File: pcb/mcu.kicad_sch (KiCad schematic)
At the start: 28 parts, among them U1 W25Q128JVS, U2 RP2040, Y1 ABM8AIG-12.000MHZ-12-2Z-T3

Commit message: Start routing rev. A
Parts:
- U1: footprint Package_SO:SOIC-8_5.23x5.23mm_P1.27mm -> Package_SO:SOIC-8_5.275x5.275mm_P1.27mm
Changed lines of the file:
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@@
 			)
 		)
-		(property "Footprint" "Package_SO:SOIC-8_5.23x5.23mm_P1.27mm"
+		(property "Footprint" "Package_SO:SOIC-8_5.275x5.275mm_P1.27mm"
 			(at 38.1 72.39 0)
 			(effects

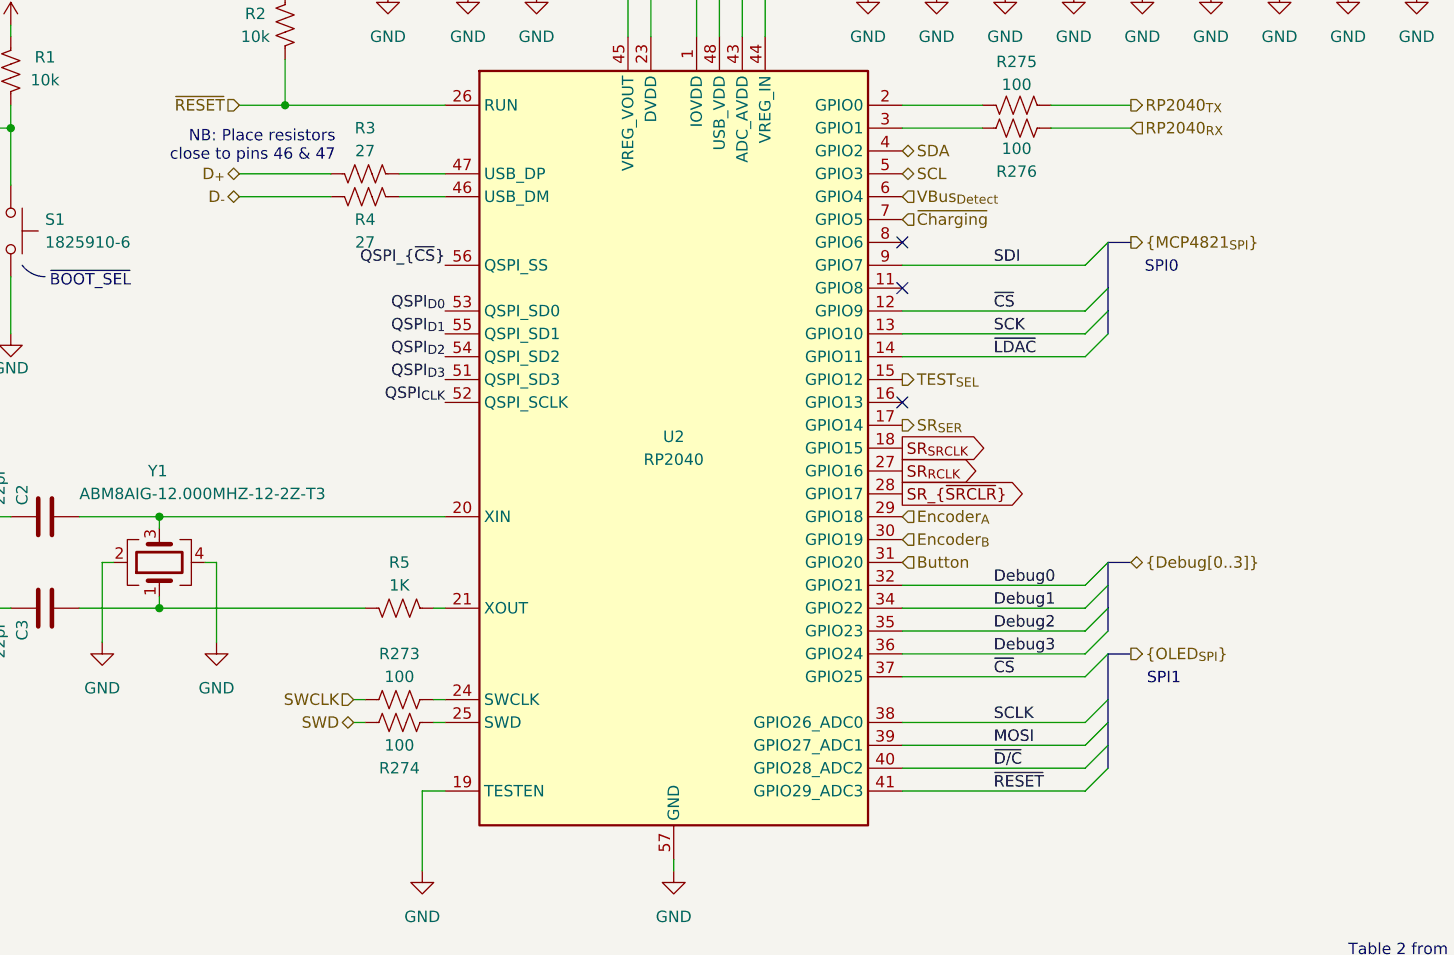
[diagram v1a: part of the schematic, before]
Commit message: Routing nearly complete
- Power switch is too tall I think
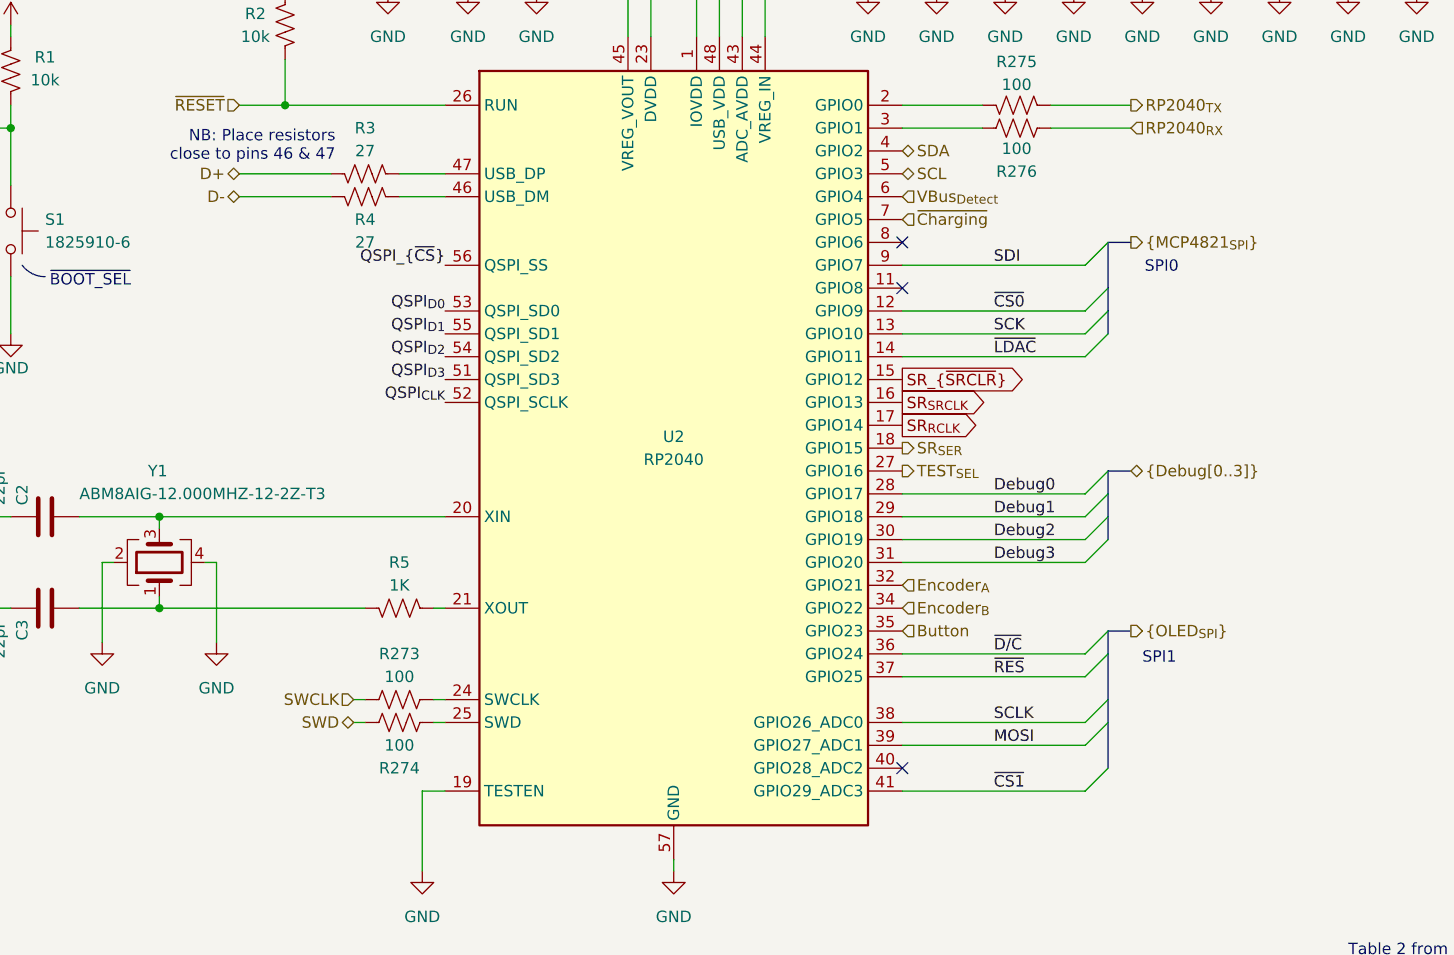
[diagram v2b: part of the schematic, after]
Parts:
- C1, C10, C11, C12, C13, C14, C5, C6, C7, C8, C9: TempCo (none) -> X7R
- C15, C4: TempCo (none) -> X5R; Voltage (none) -> 16V
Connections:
- net Button: now also U2.35 (GPIO23); no longer U2.31 (GPIO20)
- net Debug0: now also U2.28 (GPIO17); no longer U2.32 (GPIO21)
- net Debug1: now also U2.29 (GPIO18); no longer U2.34 (GPIO22)
- net Debug2: now also U2.30 (GPIO19); no longer U2.35 (GPIO23)
- net Debug3: now also U2.31 (GPIO20); no longer U2.36 (GPIO24)
- net Encoder_{A}: now also U2.32 (GPIO21); no longer U2.29 (GPIO18)
- net Encoder_{B}: now also U2.34 (GPIO22); no longer U2.30 (GPIO19)
- net SR_{RCLK}: now also U2.17 (GPIO14); no longer U2.27 (GPIO16)
- net SR_{SER}: now also U2.18 (GPIO15); no longer U2.17 (GPIO14)
- net SR_{SRCLK}: now also U2.16 (GPIO13); no longer U2.18 (GPIO15)
- net SR_{~{SRCLR}}: now also U2.15 (GPIO12); no longer U2.28 (GPIO17)
- net TEST_{SEL}: now also U2.27 (GPIO16); no longer U2.15 (GPIO12)
- net ~{D/C}: now also U2.36 (GPIO24); no longer U2.40 (GPIO28_ADC2)
- net ~{RESET}: no longer U2.41 (GPIO29_ADC3)
- net D_{+} renamed D+
- net D_{-} renamed D-
- net ~{CS} renamed ~{CS0}
- net ~{CS0}: no longer U2.37 (GPIO25)
- new net ~{CS1}: U2.41 (GPIO29_ADC3)
- new net ~{RES}: U2.37 (GPIO25)

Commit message: Rev. A of PCB
- I will make a case before fabrication so that they can be made
  together
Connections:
- net ~{Charging}: no longer names the net of U2.7 (GPIO5)
- no-connect marks 3 -> 4
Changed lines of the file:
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@@
 	)
 	(no_connect
+		(at 158.75 74.93)
+	)
+	(no_connect
 		(at 158.75 135.89)
 	)
@@
 		(fields_autoplaced yes)
 		(effects
-			(font
-				(size 1.27 1.27)
-			)
-			(justify left)
-		)
-	)
-	(hierarchical_label "~{Charging}"
-		(shape input)
-		(at 158.75 74.93 0)
-		(fields_autoplaced yes)
-		(effects

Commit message: Fix MCP73831 subcircuit
- Add decoupling capacitor on Vbat
- Add more thermal support to layout (solid connection of ground to
  ground plane copper and addition of thermal vias)
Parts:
- renumbered S1 to SW3
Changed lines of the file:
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@@
 	(title_block
 		(title "Extracellular Electrophysiology Test Board")
-		(rev "A")
+		(rev "B")
 		(company "Open Ephys, Inc")
 		(comment 1 "Jonathan P. Newman")
@@
 		(on_board yes)
 		(dnp no)
-		(property "Reference" "S1"
+		(property "Reference" "SW3"
 			(at 63.5 74.9299 90)
 			(effects
@@
 			(project "ephys-test-board"
 				(path "/ffaa6ffd-73fa-4da3-9ff1-78fa7369281f/72625ec8-68e6-44fb-ba42-4cf3e0d4f05e"
-					(reference "S1")
+					(reference "SW3")
 					(unit 1)
 				)

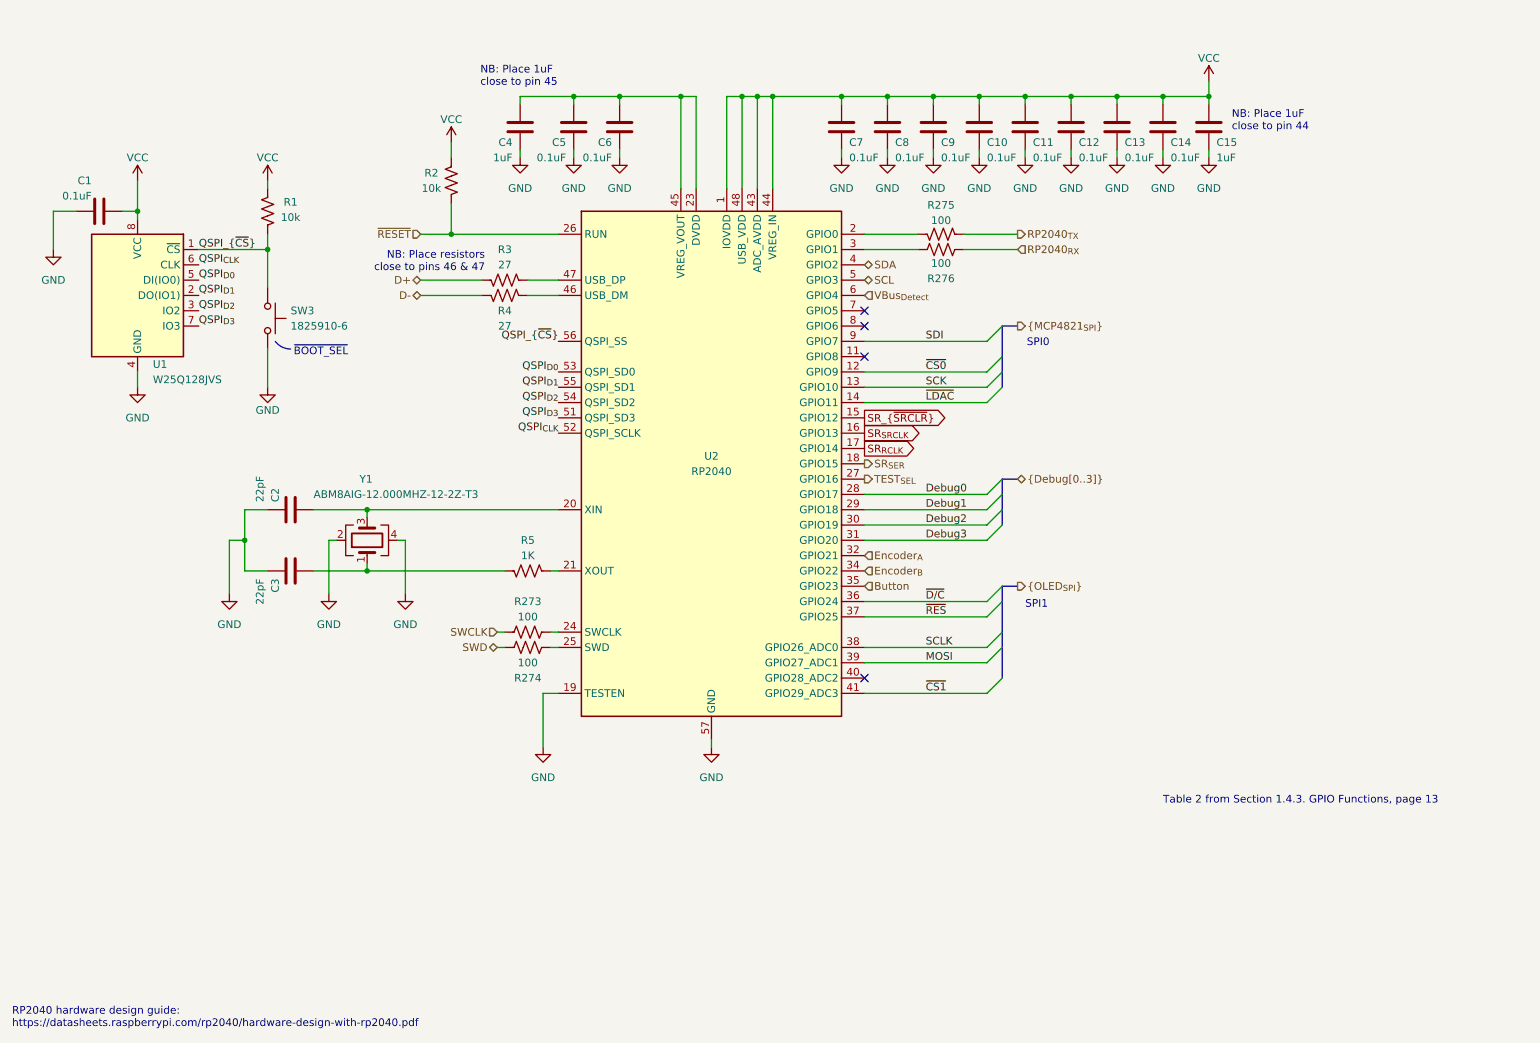
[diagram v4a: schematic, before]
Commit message: Address several issues found when testing rev. A
- Add Reset button to back panel
- Make board smaller
- Move battery to bottom of device
- Replace OLED with a more reasonable choice.
- Etc.
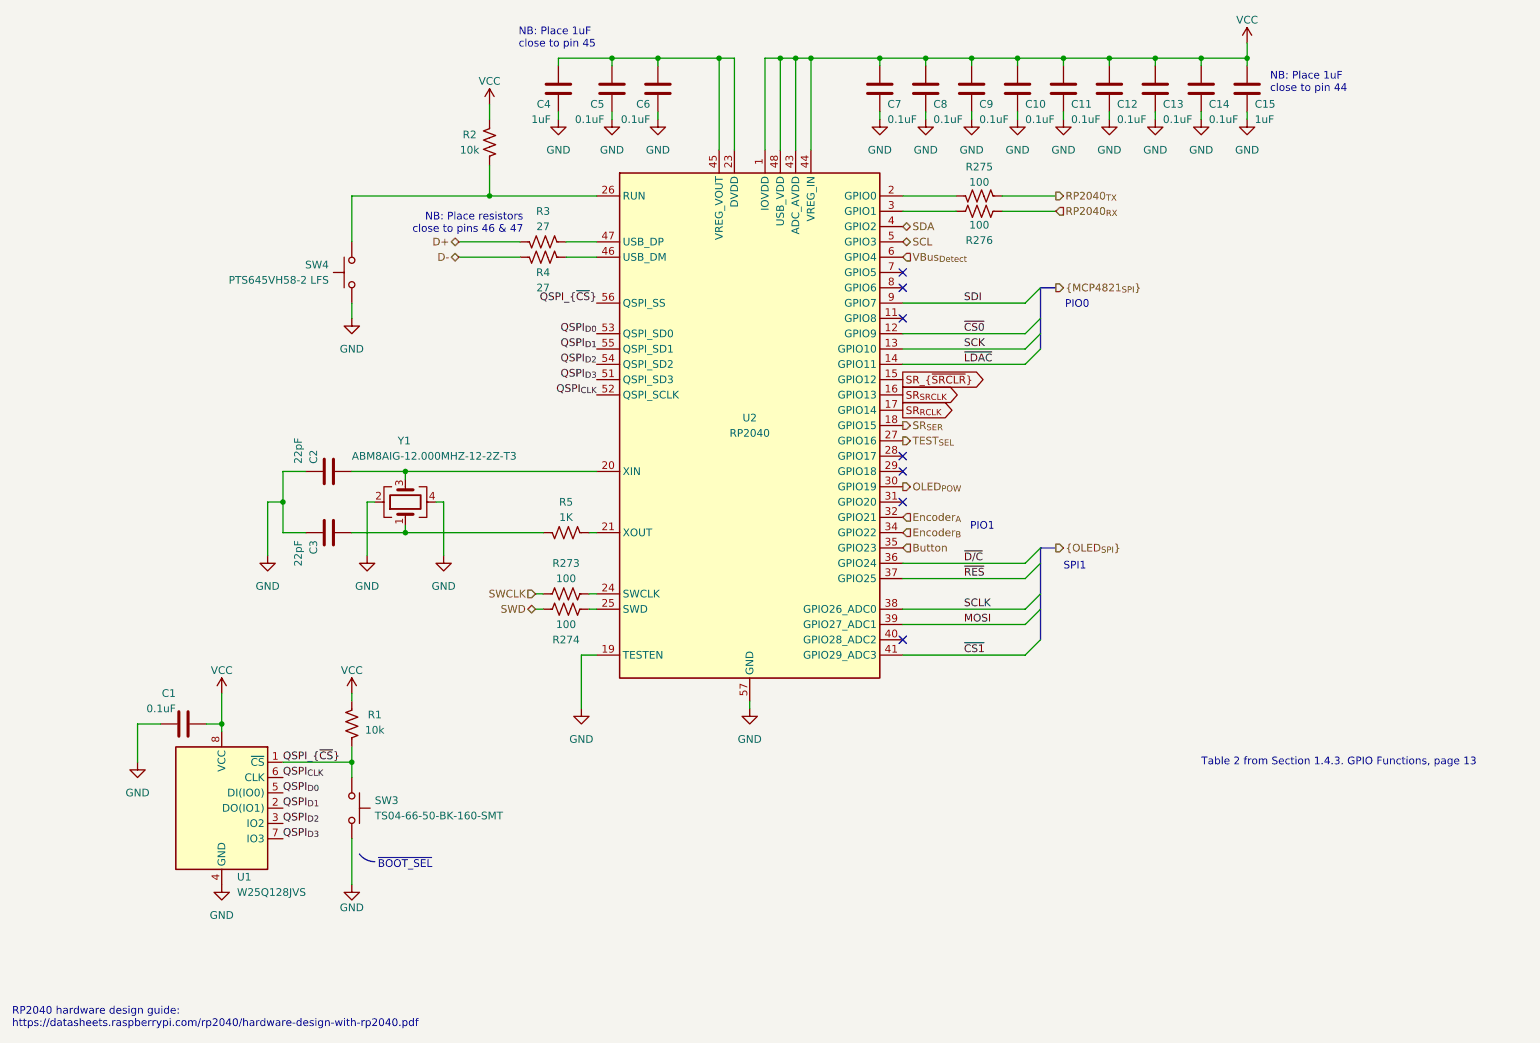
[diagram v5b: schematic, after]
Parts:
- added SW4: PTS645VH58-2 LFS, Button_Switch_THT:SW_Tactile_SPST_Angled_PTS645Vx83-2LFS, symbol Switch:SW_Push
- C2, C3: Part No. (none) -> C0402C0G500-220GNP-CT
- SW3: value 1825910-6 -> TS04-66-50-BK-160-SMT; footprint Button_Switch_THT:SW_PUSH_6mm_H4.3mm -> open-ephys:SAMESKY_TS04-66-XX-BK-XXX-SMT-XX
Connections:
- net GND: now also SW4.1
- net Debug0: no longer names the net of U2.28 (GPIO17)
- net Debug1: no longer names the net of U2.29 (GPIO18)
- net Debug2 renamed OLED_{POW}
- net Debug3: no longer names the net of U2.31 (GPIO20)
- net ~{RESET}: no longer names the net of R2.2, U2.26 (RUN)
- net ~{RESET}: now also SW4.2
- no-connect marks 4 -> 7
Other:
- note added: "PIO0"
- note added: "PIO1"
- note removed: "SPI0"
- moved on the sheet: C1, C10, C11, C12, C13, C14, C15, C2, C3, C4, C5, C6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
